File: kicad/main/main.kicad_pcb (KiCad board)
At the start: 2 copper layers, 44.5 x 35 mm, 19 parts, among them J2 Conn_01x02, J3 Conn_01x07_Pin, J4 Conn_01x04_Pin, P1 USB_C_Plug_USB2.0, SW1 MK-12C03-G015, SW3 SW_Push, SW4 SW_Push, U1 HUSB237, U2 ZX-PH2.0-WT4P

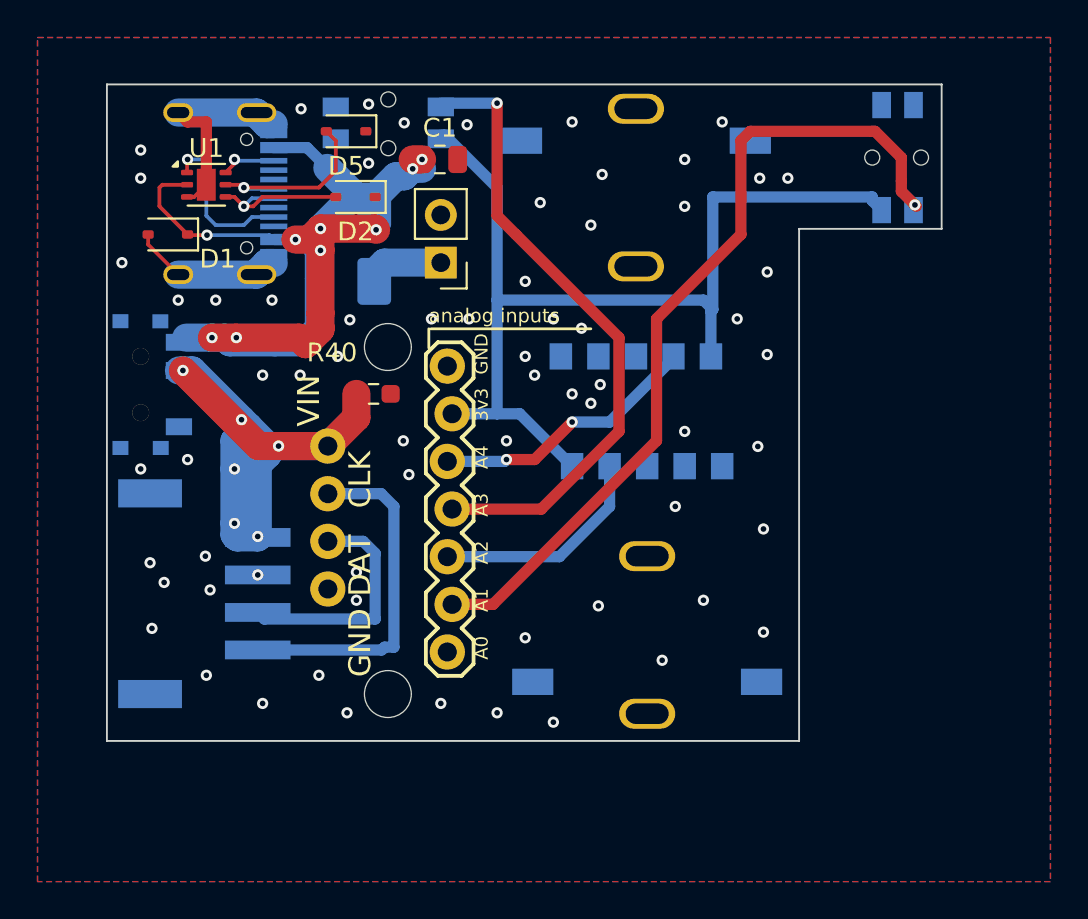
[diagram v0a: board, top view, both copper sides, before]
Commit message: New board arrangement
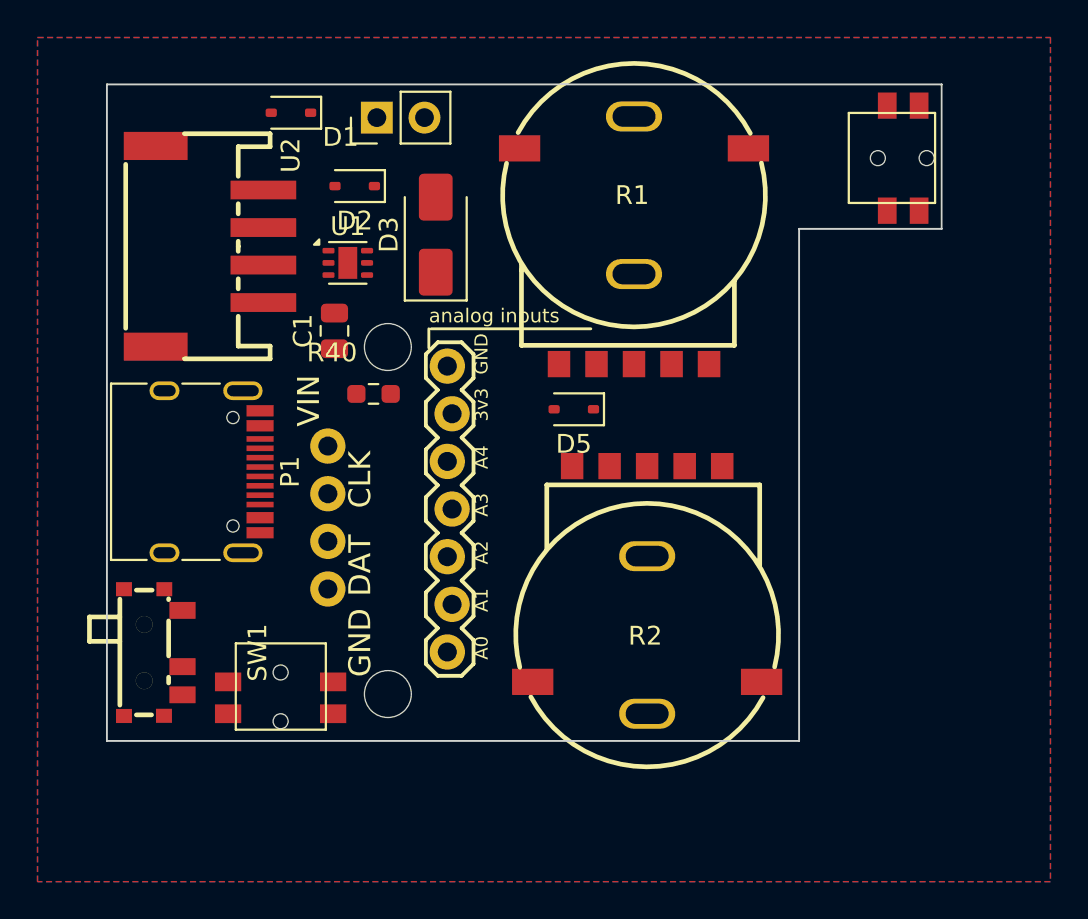
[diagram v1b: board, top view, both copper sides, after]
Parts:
- D3, P1, R1, R2, SW1, SW3, SW4, U2: moved to F.Cu
- moved SW3 43.6 mm to (170.5, 107.7), turned to 0 degrees
- moved SW4 27.5 mm to (203.6, 78.9), turned to 90 degrees
- moved D5 19.2 mm to (186.1, 92.3)
- moved U2 18.5 mm to (166.7, 83.6), turned to -90 degrees
- moved P1 14.8 mm to (165.3, 95.7), turned to -90 degrees
- moved SW1 14.3 mm to (163.7, 105.3), turned to -90 degrees
- moved C1 10.7 mm to (173.3, 88.1), turned to 90 degrees
- moved D1 9.23 mm to (171.0, 76.5)
- moved U1 8.61 mm to (174.0, 84.5)
- moved J2 8.45 mm to (175.6, 76.8), turned to 90 degrees
- moved D3 3.32 mm to (178.7, 83.0), turned to 90 degrees
- moved D2 0.58 mm to (174.4, 80.4)
- moved R1 0.42 mm to (189.3, 83.3), turned to 0 degrees
- turned R2 to 180 degrees
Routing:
- net VBUS: track 56.6 -> 0.00 mm, vias 9 -> 0
- net +3V3: track 53.4 -> 0.00 mm
- net AIN1: track 44.6 -> 0.00 mm, vias 1 -> 0
- net VIN: track 34.9 -> 0.00 mm, vias 6 -> 0
- net AIN3: track 33.8 -> 0.00 mm, vias 1 -> 0
- net GND: track 20.0 -> 0.00 mm, vias 61 -> 0
- net SCK_OUT: track 18.6 -> 0.00 mm
- net AIN4: track 14.4 -> 0.00 mm, vias 2 -> 0
- net MOSI_OUT: track 12.7 -> 0.00 mm
- net AIN2: track 11.9 -> 0.00 mm
- net D-: track 10.2 -> 0.00 mm, vias 1 -> 0
- net CC1: track 8.69 -> 0.00 mm, vias 1 -> 0
- net D+: track 8.06 -> 0.00 mm, vias 1 -> 0
- net Net-(D3-A): track 3.71 -> 0.00 mm
- net CC2: track 3.06 -> 0.00 mm, vias 1 -> 0
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
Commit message: Rewired PCB
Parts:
- D3: value SS34 -> 1N4007; footprint Diode_SMD:D_SMA -> Diode_THT:D_DO-41_SOD81_P10.16mm_Horizontal
- moved SW3 30.8 mm to (176.2, 77.4), turned to 180 degrees
- moved D1 21.9 mm to (169.8, 98.3), turned to 90 degrees
- moved D2 21.8 mm to (176.0, 102.1), turned to 0 degrees
- moved U1 20.8 mm to (169.9, 104.9), turned to 180 degrees
- moved C1 20.2 mm to (172.0, 108.3), turned to 0 degrees
- moved D3 17.7 mm to (166.9, 96.2), turned to 60 degrees
- moved D5 16.1 mm to (175.9, 104.8), turned to 0 degrees
- moved SW1 11.7 mm to (162.5, 93.6)
- moved P1 8.97 mm to (162.6, 104.2)
- moved J2 7.48 mm to (175.7, 84.2)
- moved U2 2.54 mm to (165.1, 81.6)
- moved R1 0.46 mm to (189.6, 83.0)
- moved R2 0.23 mm to (189.8, 102.1)
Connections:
- D2 pad 1: GND -> D+
- D2 pad 2: D+ -> GND
- D5 pad 1: GND -> D-
- D5 pad 2: D- -> GND
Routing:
- net +3V3: track 0.00 -> 68.0 mm, vias 0 -> 3
- net AIN1: track 0.00 -> 39.9 mm, vias 0 -> 1
- net AIN3: track 0.00 -> 39.8 mm
- net VBUS: track 0.00 -> 30.6 mm
- net SCK_OUT: track 0.00 -> 28.0 mm, vias 0 -> 1
- net MOSI_OUT: track 0.00 -> 26.4 mm, vias 0 -> 1
- net D-: track 0.00 -> 23.6 mm, vias 0 -> 2
- net VIN: track 0.00 -> 22.5 mm
- net D+: track 0.00 -> 19.4 mm, vias 0 -> 2
- net AIN2: track 0.00 -> 15.5 mm
- net AIN4: track 0.00 -> 11.3 mm
- net CC1: track 0.00 -> 7.58 mm, vias 0 -> 2
- net Net-(D3-A): track 0.00 -> 5.00 mm
- net CC2: track 0.00 -> 2.47 mm
- net GND: vias 0 -> 3
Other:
- board size 44.5 x 35 mm -> 45.7 x 35 mm

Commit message: Rewired PCB
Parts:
- moved C1 1.21 mm to (173.0, 107.6), turned to -90 degrees
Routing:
- net VIN: track 22.5 -> 37.9 mm, vias 0 -> 7
- net VBUS: track 30.6 -> 40.5 mm, vias 0 -> 12
- net +3V3: track 68.0 -> 76.3 mm
- net GND: track 0.00 -> 4.82 mm, vias 3 -> 39
